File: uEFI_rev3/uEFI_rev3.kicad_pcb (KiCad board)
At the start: 4 copper layers, 99.9 x 123 mm, 219 parts, among them J1 USB_B, J2 Tag connect, J3 36638-0002, J4 Conn_02x08_Odd_Even, Q1 ISL9V5045S3ST, Q10 IRF540N, Q11 SS8050, Q12 AO3400A, Q2 ISL9V5045S3ST, Q3 ISL9V5045S3ST, Q4 ISL9V5045S3ST, Q5 SS8050, Q6 IRF540N, Q7 IRF540N, Q8 SS8050, Q9 SS8050, SW1 SW_Push, U1 MCZ33810EK, U10 SensorsV2, U11 SensorsV2, U12 SensorsV2, U13 SensorsV2, U14 SensorsV2, U15 TJA1042T3118, U2 SensorsV2, U20 TPL7407LAPWR, U22 TPL7407LAPWR, U23 PaP_Driver_v1, U27 LM321, U3 STM32F407VGTx, U31 LM321, U36 MAX9926UAEE+, U4 MIC2940A-3.3WU, U5 MIC2940A-5.0WT, U6 LT4363IMS, U7 25LCxxx, U8 SensorsV2, U9 SensorsV2, Y1 25MHz

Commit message: rev3, analog inputs
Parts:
- removed D14: DZ2S033X0L, Diode_SMD:D_MiniMELF
- removed the H9 at (60.7, 115.8)
- removed the H9 at (110.2, 115.6)
- removed the H9 at (64.8, 49.3)
- removed JP11, JP19: Jumper_NC_Small, Jumper:SolderJumper-2_P1.3mm_Open_TrianglePad1.0x1.5mm
- removed TP10, TP11, TP12, TP13, TP14, TP15, TP16, TP17: TestPoint, TestPoint:TestPoint_Pad_2.0x2.0mm
- removed U10, U11, U12, U13, U14: SensorsV2, OpenEFI-STM32F_rev3:Sensors_v2
- added C1: 240pF, Capacitor_SMD:C_0603_1608Metric, F.Cu at (133.1, 126.3)
- added C32: 240pF, Capacitor_SMD:C_0603_1608Metric, F.Cu at (133.1, 136.1)
- added C35: 240pF, Capacitor_SMD:C_0603_1608Metric, F.Cu at (144.4, 136.1)
- added C37: 240pF, Capacitor_SMD:C_0603_1608Metric, F.Cu at (133.1, 146.0)
- added C38: 240pF, Capacitor_SMD:C_0603_1608Metric, F.Cu at (144.4, 146.0)
- added C39: 100nF, Capacitor_SMD:C_0805_2012Metric, F.Cu at (161.7, 124.1)
- added C4: 240pF, Capacitor_SMD:C_0603_1608Metric, F.Cu at (144.4, 126.3)
- added C40: 4.7uF, Capacitor_SMD:C_0805_2012Metric, F.Cu at (170.0, 129.1)
- added D15: K26, Diode_SMD:D_SOD-123F, F.Cu at (149.4, 126.7)
- added D16: K26, Diode_SMD:D_SOD-123F, F.Cu at (138.0, 126.7)
- added D17: K26, Diode_SMD:D_SOD-123F, F.Cu at (65.5, 84.8)
- added D19: K26, Diode_SMD:D_SOD-123F, F.Cu at (138.0, 124.1)
- added D20: K26, Diode_SMD:D_SOD-123F, F.Cu at (70.6, 83.9)
- added D21: K26, Diode_SMD:D_SOD-123F, F.Cu at (138.0, 136.5)
- added D22: K26, Diode_SMD:D_SOD-123F, F.Cu at (149.3, 136.5)
- added D23: K26, Diode_SMD:D_SOD-123F, F.Cu at (138.0, 134.0)
- added D24: K26, Diode_SMD:D_SOD-123F, F.Cu at (149.3, 134.0)
- added D25: K26, Diode_SMD:D_SOD-123F, F.Cu at (125.6, 131.4)
- added D26: K26, Diode_SMD:D_SOD-123F, F.Cu at (138.0, 146.4)
- added D27: K26, Diode_SMD:D_SOD-123F, F.Cu at (149.4, 146.4)
- added D28: K26, Diode_SMD:D_SOD-123F, F.Cu at (128.0, 131.4)
- added D29: K26, Diode_SMD:D_SOD-123F, F.Cu at (138.0, 143.8)
- added D30: K26, Diode_SMD:D_SOD-123F, F.Cu at (149.4, 143.8)
- added JP10: Jumper_NC_Small, Jumper:SolderJumper-2_P1.3mm_Open_TrianglePad1.0x1.5mm, F.Cu at (149.9, 141.2)
- added JP12: Jumper_NC_Small, Jumper:SolderJumper-2_P1.3mm_Open_TrianglePad1.0x1.5mm, F.Cu at (127.3, 136.4)
- added JP5: Jumper_NC_Small, Jumper:SolderJumper-2_P1.3mm_Open_TrianglePad1.0x1.5mm, F.Cu at (138.6, 121.5)
- added JP6: Jumper_NC_Small, Jumper:SolderJumper-2_P1.3mm_Open_TrianglePad1.0x1.5mm, F.Cu at (149.9, 121.5)
- added JP7: Jumper_NC_Small, Jumper:SolderJumper-2_P1.3mm_Open_TrianglePad1.0x1.5mm, F.Cu at (138.6, 131.3)
- added JP8: Jumper_NC_Small, Jumper:SolderJumper-2_P1.3mm_Open_TrianglePad1.0x1.5mm, F.Cu at (149.9, 131.3)
- added JP9: Jumper_NC_Small, Jumper:SolderJumper-2_P1.3mm_Open_TrianglePad1.0x1.5mm, F.Cu at (138.6, 141.2)
- added R36: 28.6k +-1%, Resistor_SMD:R_0603_1608Metric, F.Cu at (131.4, 126.3)
- added R37: 28.6k +-1%, Resistor_SMD:R_0603_1608Metric, F.Cu at (142.7, 126.3)
- added R38: 2.2k, Resistor_SMD:R_0603_1608Metric, F.Cu at (135.3, 121.5)
- added R39: 2.2k, Resistor_SMD:R_0603_1608Metric, F.Cu at (146.6, 121.5)
- added R40: 3.32k +-1%, Resistor_SMD:R_0603_1608Metric, F.Cu at (134.7, 126.3)
- added R41: 3.32k +-1%, Resistor_SMD:R_0603_1608Metric, F.Cu at (146.2, 126.3)
- added R42: 28.6k +-1%, Resistor_SMD:R_0603_1608Metric, F.Cu at (131.4, 136.1)
- added R43: 28.6k +-1%, Resistor_SMD:R_0603_1608Metric, F.Cu at (142.7, 136.1)
- added R44: 2.2k, Resistor_SMD:R_0603_1608Metric, F.Cu at (135.3, 131.3)
- added R45: 2.2k, Resistor_SMD:R_0603_1608Metric, F.Cu at (146.6, 131.3)
- added R46: 0, Resistor_SMD:R_0603_1608Metric, F.Cu at (117.6, 139.1)
- added R47: 3.32k +-1%, Resistor_SMD:R_0603_1608Metric, F.Cu at (134.9, 136.1)
- added R48: 3.32k +-1%, Resistor_SMD:R_0603_1608Metric, F.Cu at (146.2, 136.1)
- added R49: 28.6k +-1%, Resistor_SMD:R_0603_1608Metric, F.Cu at (131.4, 146.0)
- added R50: 28.6k +-1%, Resistor_SMD:R_0603_1608Metric, F.Cu at (142.7, 146.0)
- added R51: 2.2k, Resistor_SMD:R_0603_1608Metric, F.Cu at (135.3, 141.2)
- added R52: 2.2k, Resistor_SMD:R_0603_1608Metric, F.Cu at (146.6, 141.2)
- added R53: 3.32k +-1%, Resistor_SMD:R_0603_1608Metric, F.Cu at (134.9, 146.0)
- added R54: 3.32k +-1%, Resistor_SMD:R_0603_1608Metric, F.Cu at (146.2, 146.0)
- added R55: 10k, Resistor_SMD:R_0603_1608Metric, F.Cu at (164.5, 124.3)
- added RV1: 2k, Potentiometer_THT:Potentiometer_Bourns_3386C_Horizontal, F.Cu at (163.2, 139.4)
- D18: value DZ2S033X0L -> K26; footprint Diode_SMD:D_MiniMELF -> Diode_SMD:D_SOD-123F
- R18: moved to B.Cu
- U2: value SensorsV2 -> MCP3208; footprint OpenEFI-STM32F_rev3:Sensors_v2 -> Package_SO:SOIC-16_3.9x9.9mm_P1.27mm
- U8: value SensorsV2 -> LM4040DBZ-5; footprint OpenEFI-STM32F_rev3:Sensors_v2 -> Package_TO_SOT_SMD:SOT-23
- U9: value SensorsV2 -> AMS1117-5.0; footprint OpenEFI-STM32F_rev3:Sensors_v2 -> Package_TO_SOT_SMD:SOT-223-3_TabPin2
- moved D18 82.7 mm to (149.4, 124.1)
- moved Q11 52.4 mm to (123.2, 126.0)
- moved Q12 52.1 mm to (127.3, 126.0)
- moved R34 51.9 mm to (120.1, 126.5), turned to -90 degrees
- moved D11 51.7 mm to (127.5, 120.7)
- moved R35 48.9 mm to (123.3, 122.4)
- moved U9 30.5 mm to (164.3, 131.3)
- moved U8 29.1 mm to (170.7, 133.7)
- moved C16 24.9 mm to (81.0, 146.6)
- moved J2 24.4 mm to (84.5, 159.0)
- moved H5 17.6 mm to (125.0, 152.9)
- moved TP19 15.9 mm to (120.5, 131.9)
- moved R32 15.8 mm to (101.2, 148.7), turned to -90 degrees
- moved C51 15.4 mm to (122.8, 133.1)
- moved U27 15.3 mm to (123.5, 135.9)
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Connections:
- net Net-(JP11-Pad1) renamed /Sensores/CH7
- C29 pad 2: M4 -> M3
- C30 pad 2: M3 -> M4
- C49 pad 1: B1 -> K1
- C49 pad 2: GND -> GNDA
- C51 pad 2: GND -> GNDA
- D18 pad 1: Net-(D18-Pad1) -> /Sensores/CH1
- D18 pad 2: GND -> GNDA
- JP15 pad 2: Net-(D18-Pad1) -> /Sensores/CH6
- JP18 pad 1: Net-(D18-Pad1) -> /Sensores/CH6
- R109 pad 1: GND -> GNDA
- R83 pad 2: GND -> GNDA
- R87 pad 1: B1 -> K1
- R87 pad 2: GND -> GNDA
- R92 pad 1: B1 -> K1
- R92 pad 2: +5V -> +5C
- R97 pad 2: B1 -> K1
- TP18 pad 1: Net-(D18-Pad1) -> /Sensores/CH6
- U1 pad 1: M3 -> M4
- U1 pad 16: M4 -> M3
- U2 pad 1: +5VA -> Net-(JP5-Pad2)
- U2 pad 2: +12V -> Net-(JP6-Pad2)
- U2 pad 3: K1 -> Net-(JP7-Pad2)
- U2 pad 4: /Sensores/PA0 -> Net-(JP8-Pad2)
- U2 pad 5: GND -> Net-(JP9-Pad2)
- U27 pad 2: GND -> GNDA
- U27 pad 5: +5V -> +5C
- U3 pad 15: /Sensores/PC0 -> /ADC_CS
- U3 pad 23: /Sensores/PA0 -> /PA0
- U3 pad 24: /Sensores/PA1 -> /PA1
- U3 pad 25: /Sensores/PA2 -> /PA2
- U3 pad 26: /Sensores/PA3 -> /PA3
- U3 pad 29: /Sensores/PA4 -> /PA4
- U3 pad 30: /Sensores/PA5 -> /PA5
- U3 pad 31: /Sensores/PA6 -> /PA6
- U3 pad 32: /Sensores/PA7 -> /PA7
- U3 pad 34: /Sensores/PC5 -> unconnected-(U3-Pad34)
- U31 pad 2: GND -> GNDA
- U31 pad 4: Net-(D18-Pad1) -> /Sensores/CH6
- U8 pad 1: +5VA -> +5VL
- U8 pad 2: +12V -> GNDA
- U8 pad 3: E1 -> (no net)
- U9 pad 1: +5VA -> Net-(C39-Pad1)
- U9 pad 2: +12V -> +5C
- U9 pad 3: H1 -> +12V
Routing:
- net F1: track 0.00 -> 111.6 mm, vias 0 -> 1
- net G1: track 0.00 -> 104.5 mm, vias 0 -> 2
- net D1: track 0.00 -> 93.7 mm, vias 0 -> 2
- net E1: track 0.00 -> 90.5 mm, vias 0 -> 1
- net GND: track 34.8 -> 112.0 mm, vias 14 -> 18
- net A1: track 0.00 -> 73.4 mm, vias 0 -> 2
- net B1: track 0.00 -> 73.3 mm, vias 0 -> 1
- net Net-(C22-Pad2): track 0.00 -> 71.8 mm
- net C1: track 0.00 -> 71.3 mm, vias 0 -> 1
- net M4: track 0.00 -> 54.0 mm
- net L4: track 0.00 -> 52.4 mm
- net M3: track 0.00 -> 48.1 mm
- net L3: track 0.00 -> 47.5 mm
- net Net-(JP6-Pad2): track 0.00 -> 41.0 mm
- net Net-(JP8-Pad2): track 0.00 -> 37.1 mm
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- added copper zone on In1.Cu, net +5C
- added copper zone on F.Cu, net GNDA
- removed copper zone on B.Cu, net GND
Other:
- board text added: "A0"
- board text added: "A1"
- board text added: "A2"
- board text added: "A3"
- board text added: "A4"
- board text added: "A5"
- board text removed: "EN"

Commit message: rev3 ADC SPI
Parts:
- removed RV1: 2k, Potentiometer_THT:Potentiometer_Bourns_3386C_Horizontal
- added R56: 750, Resistor_SMD:R_0603_1608Metric, F.Cu at (113.9, 144.8)
- added R57: 220, Resistor_SMD:R_0603_1608Metric, F.Cu at (112.3, 144.8)
- added U10: TXS0102DCU, Package_SO:VSSOP-8_2.3x2mm_P0.5mm, F.Cu at (104.4, 139.8)
- added U11: TXS0102DCU, Package_SO:VSSOP-8_2.3x2mm_P0.5mm, F.Cu at (104.4, 142.6)
- U9: value AMS1117-5.0 -> AMS1117
- moved C40 54.6 mm to (115.4, 132.7), turned to 0 degrees
- moved U9 51.3 mm to (113.5, 138.4)
- moved R55 50.8 mm to (122.3, 152.8)
- moved C39 50.3 mm to (116.0, 144.9), turned to -90 degrees
- moved U8 49.4 mm to (125.0, 152.5)
- moved H5 24.7 mm to (149.6, 150.7)
- moved R46 12.9 mm to (125.9, 149.0), turned to -90 degrees
- moved C13 12.0 mm to (64.8, 137.4)
- moved C11 8.28 mm to (62.9, 122.7)
- moved C2 6.26 mm to (71.5, 118.9)
- moved C10 5.73 mm to (87.3, 126.8)
- moved C5 4.71 mm to (85.3, 139.5)
- moved J4 3.49 mm to (62.0, 143.4)
- moved C3 2.72 mm to (78.8, 118.8)
- moved SYM1 1.48 mm to (122.4, 157.9)
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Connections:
- U2 pad 10: /ADC_CS -> /Sensores/CS
- U2 pad 11: /SPI2_MOSI -> /Sensores/DIN
- U2 pad 12: /SPI2_MISO -> /Sensores/DOUT
- U2 pad 13: /SPI2_SCK -> /Sensores/CLK
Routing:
- net /Sensores/DOUT: track 0.00 -> 25.2 mm, vias 0 -> 2
- net /Sensores/CS: track 0.00 -> 23.1 mm, vias 0 -> 2
- net /Sensores/CLK: track 0.00 -> 23.0 mm, vias 0 -> 2
- net /CHK: track 0.00 -> 21.8 mm
- net +5C: track 21.0 -> 40.8 mm, vias 13 -> 14
- net /Sensores/DIN: track 0.00 -> 19.8 mm, vias 0 -> 2
- net GNDA: track 13.3 -> 31.5 mm, vias 2 -> 3
- net +5VL: track 0.00 -> 13.4 mm
- net Net-(C39-Pad1): track 0.00 -> 10.2 mm, vias 0 -> 2
- net GND: track 112.0 -> 118.7 mm, vias 18 -> 22
- net /MIL: track 0.00 -> 4.64 mm
- net Net-(D12-Pad1): track 0.00 -> 2.42 mm
- net Net-(Q8-Pad1): track 0.00 -> 1.86 mm
- net Net-(Q9-Pad1): track 0.00 -> 1.83 mm
- net Net-(D13-Pad1): track 0.00 -> 1.77 mm
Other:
- board text added: "ADC VREF"
- board text added: "OTC se la come"
- board text added: "SPI 5v/3v"

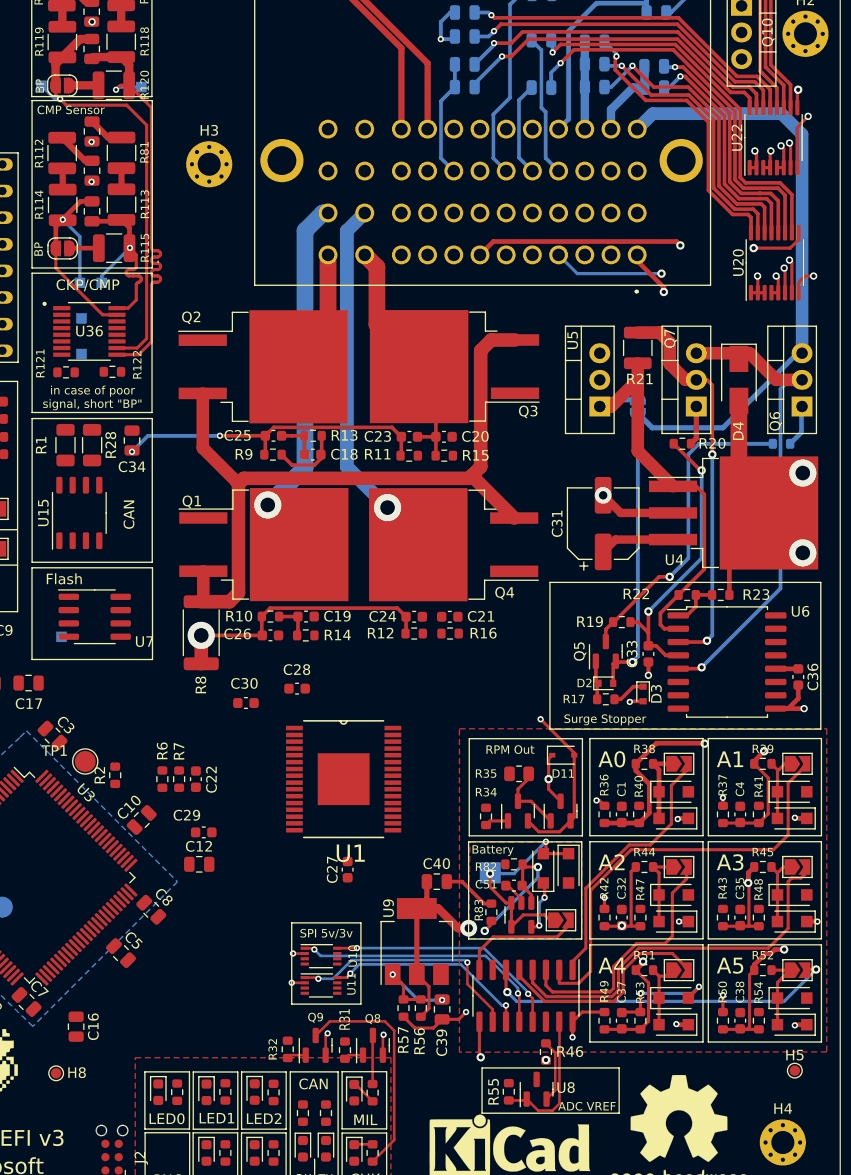
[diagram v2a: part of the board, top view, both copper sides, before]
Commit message: rev3, connect PMIC to injector outs
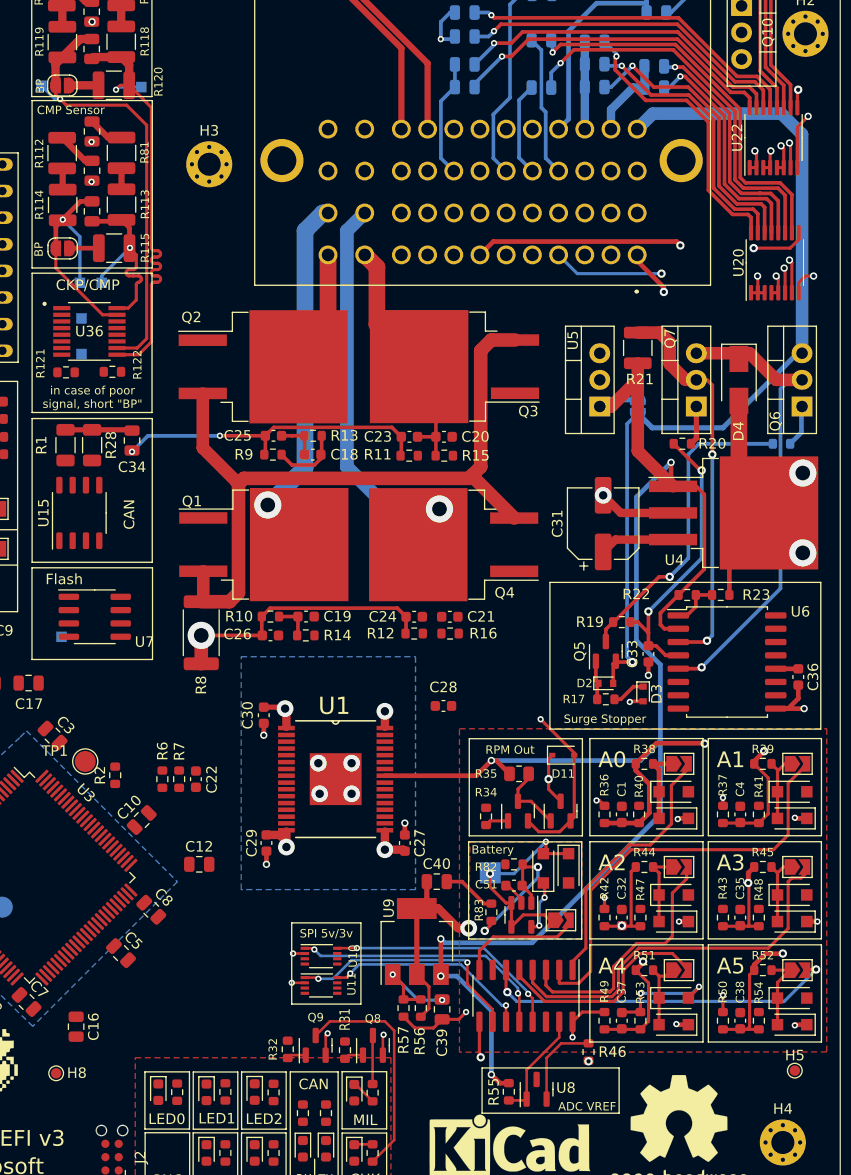
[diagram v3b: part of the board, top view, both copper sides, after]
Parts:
- moved C28 14.1 mm to (116.1, 116.0)
- moved C29 6.07 mm to (99.2, 129.0), turned to 90 degrees
- moved C27 6.02 mm to (112.4, 129.0), turned to -90 degrees
- moved R46 4.06 mm to (129.9, 149.0)
- moved C30 2.06 mm to (98.9, 116.8), turned to 90 degrees
- moved U1 0.76 mm to (105.8, 122.9)
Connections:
- C27 pad 2: L4 -> L3
- C28 pad 2: L3 -> L4
- U1 pad 17: L4 -> L3
- U1 pad 32: L3 -> L4
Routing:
- net +12V: track 87.2 -> 199.3 mm, vias 2 -> 7
- net L3: track 47.5 -> 70.5 mm, vias 0 -> 1
- net M3: track 48.1 -> 70.3 mm, vias 0 -> 1
- net M4: track 54.0 -> 60.9 mm, vias 0 -> 1
- net Net-(C34-Pad1): track 0.00 -> 6.38 mm
- net L4: track 52.4 -> 57.8 mm, vias 0 -> 1
- net L2: track 30.4 -> 35.4 mm
- net GND: track 118.7 -> 122.3 mm, vias 22 -> 29
- net +5VL: track 13.4 -> 10.5 mm
- net GNDA: track 31.5 -> 34.0 mm
- added copper zone on B.Cu, net GND
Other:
- board text removed: "OTC se la come"

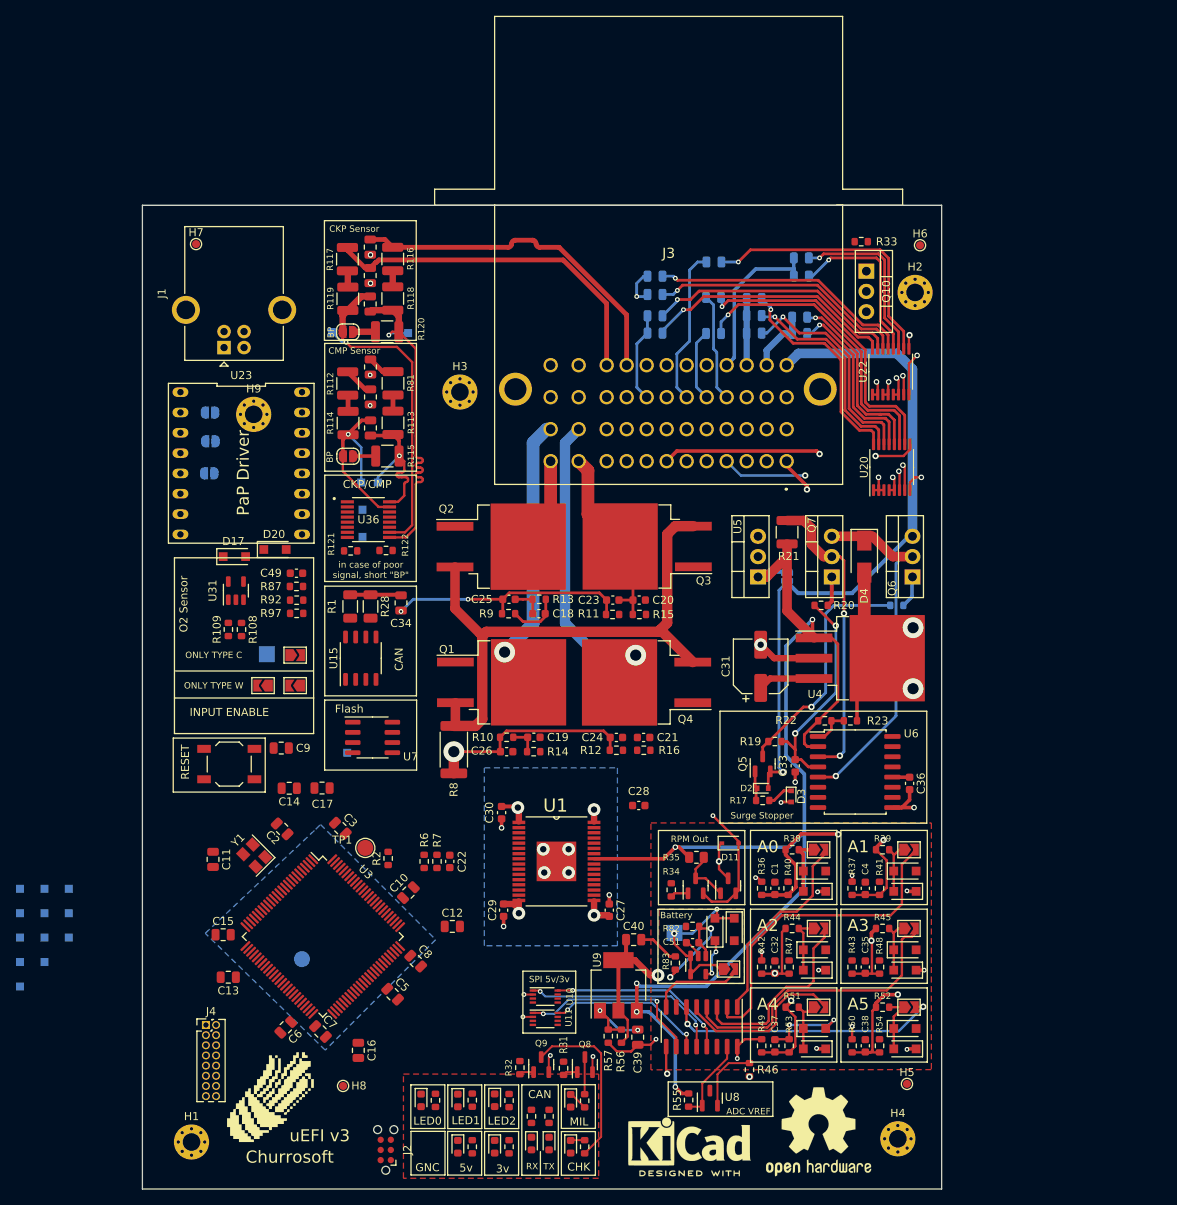
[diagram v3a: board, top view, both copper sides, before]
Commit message: rev3, PMIC, Relays done
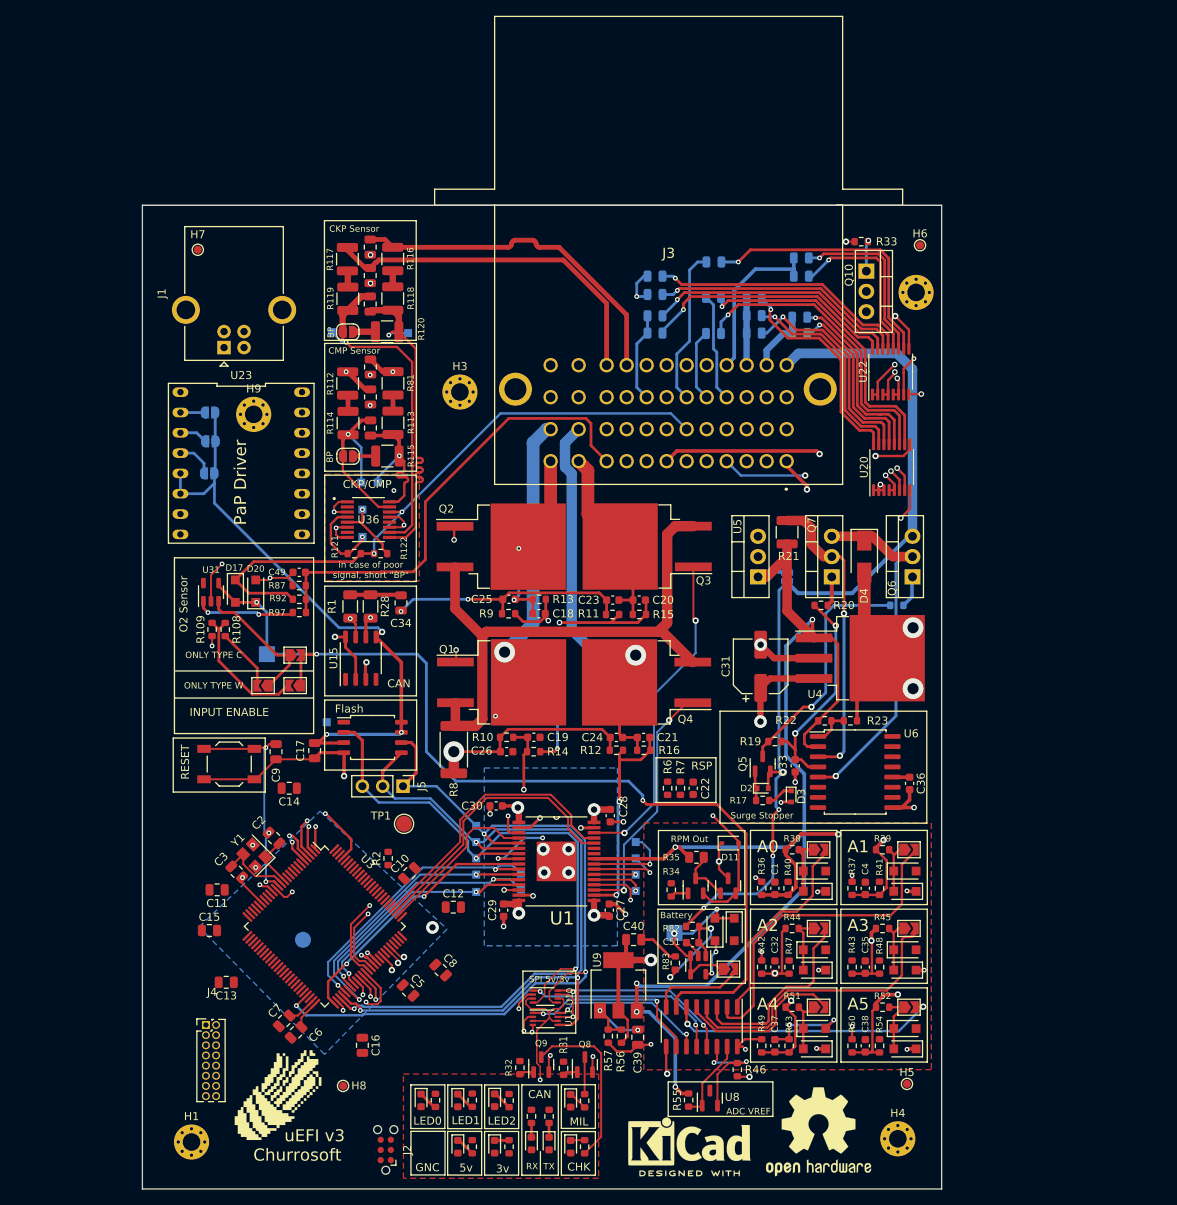
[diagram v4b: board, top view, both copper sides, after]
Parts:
- removed TP31: TestPoint, TestPoint:TestPoint_Pad_1.0x1.0mm
- added J5: Conn_01x03, Connector_PinHeader_2.54mm:PinHeader_1x03_P2.54mm_Vertical, F.Cu at (86.6, 113.5)
- H2: moved to B.Cu
- U7: footprint Package_SO:SOIC-8_3.9x4.9mm_P1.27mm -> Package_SO:SOIC-8_5.275x5.275mm_P1.27mm
- moved TP26 77.1 mm to (115.7, 124.6)
- moved TP25 74.6 mm to (115.7, 122.6)
- moved TP27 74.4 mm to (115.7, 126.6)
- moved TP24 74.4 mm to (115.7, 120.5)
- moved TP22 63.8 mm to (101.3, 126.5)
- moved TP20 63.6 mm to (101.3, 124.5)
- moved TP30 57.9 mm to (95.8, 122.6)
- moved TP28 57.6 mm to (95.8, 118.5)
- moved TP21 54.0 mm to (95.8, 124.6)
- moved TP29 52.3 mm to (95.8, 120.5)
- moved TP23 51.0 mm to (95.8, 126.7)
- moved C22 31.8 mm to (122.9, 113.8)
- moved R6 31.8 mm to (119.7, 113.8)
- moved R7 31.8 mm to (121.3, 113.8)
- moved C3 14.1 mm to (65.8, 124.2), turned to -45 degrees
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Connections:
- C49 pad 2: GNDA -> GND
- D17 pad 1: +5C -> +5VA
- D20 pad 2: GNDA -> GND
- R109 pad 1: GNDA -> GND
- R87 pad 2: GNDA -> GND
- R92 pad 2: +5C -> +5VA
- U3 pad 23: /PA0 -> /AUX_IN_1
- U3 pad 24: /PA1 -> /AUX_IN_2
- U3 pad 25: /PA2 -> /AUX_IN_3
- U3 pad 26: /PA3 -> /AUX_IN_4
- U3 pad 43: /PMIC_CS -> unconnected-(U3-Pad43)
- U3 pad 77: unconnected-(U3-Pad77) -> /PMIC_CS
- U3 pad 83: /AUX_IN_1 -> unconnected-(U3-Pad83)
- U3 pad 84: /AUX_IN_2 -> unconnected-(U3-Pad84)
- U3 pad 85: /AUX_IN_3 -> unconnected-(U3-Pad85)
- U3 pad 86: /AUX_IN_4 -> unconnected-(U3-Pad86)
- U31 pad 2: GNDA -> GND
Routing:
- net +3V3: track 7.16 -> 183.9 mm, vias 0 -> 8
- net 5V_ENABLE: track 0.00 -> 155.2 mm, vias 0 -> 2
- net /CHK_OUT: track 2.39 -> 139.9 mm, vias 1 -> 2
- net /MIL_OUT: track 3.21 -> 138.7 mm, vias 1 -> 2
- net /R_LMB: track 2.40 -> 130.4 mm, vias 1 -> 2
- net /R_AAC: track 2.31 -> 129.3 mm, vias 1 -> 2
- net /Sensores/CH6: track 0.00 -> 123.9 mm, vias 0 -> 3
- net /R_GNC_GLP: track 2.27 -> 126.1 mm, vias 1 -> 2
- net /R_ECN_INY: track 2.84 -> 123.6 mm, vias 1 -> 2
- net /TIM9_CH2: track 2.32 -> 112.2 mm, vias 1 -> 2
- net /TIM9_CH1: track 2.90 -> 110.2 mm, vias 1 -> 2
- net /SPI2_SCK: track 0.00 -> 104.3 mm, vias 0 -> 3
- net /SPI2_MISO: track 0.00 -> 103.1 mm, vias 0 -> 3
- net /SPI2_MOSI: track 0.00 -> 97.1 mm, vias 0 -> 3
- net /VBUS: track 0.00 -> 91.6 mm, vias 0 -> 1
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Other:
- board text added: "RSP"
